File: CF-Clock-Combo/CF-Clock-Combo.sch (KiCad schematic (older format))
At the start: 15 parts, among them J1 IDE_CONNECTOR, J2 CF Adapter Power, J3 Jumpers, J4 Bus_ISA_8bit, U1 BIOS FLASH, U2 74HCT245, U3 GAL22V10, U4 DS1315, Y1 32.768 KHz

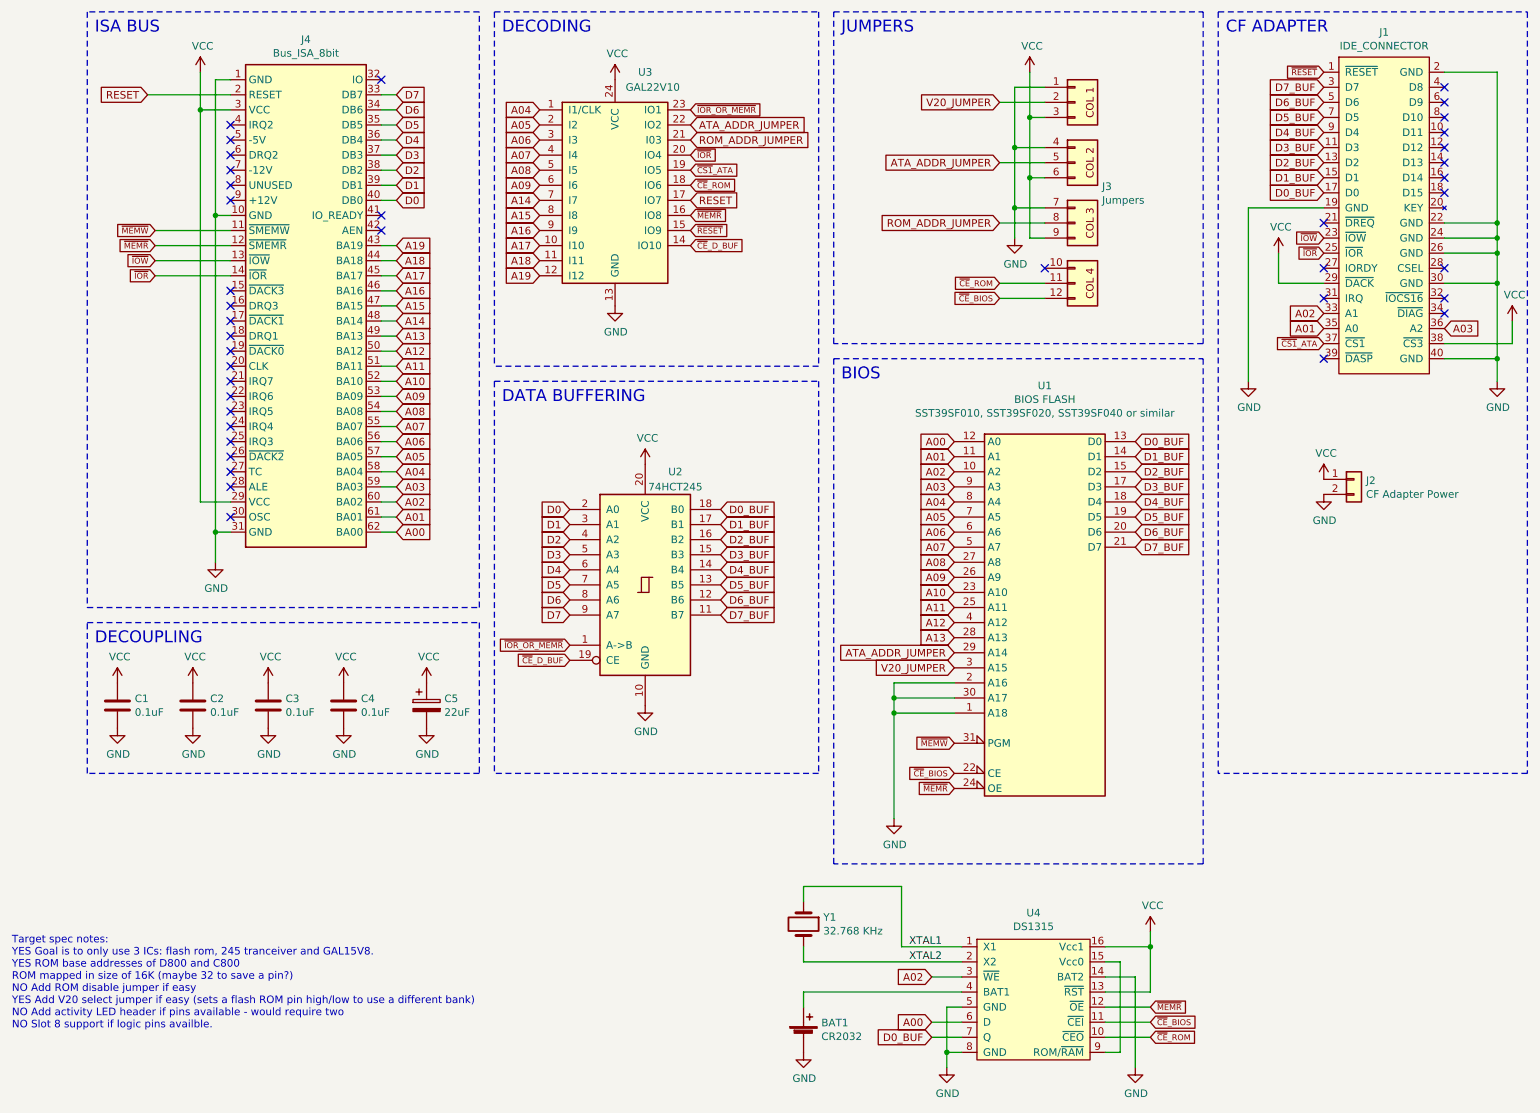
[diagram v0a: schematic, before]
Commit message: CF-Clock-Combo: Tidy up schematic.
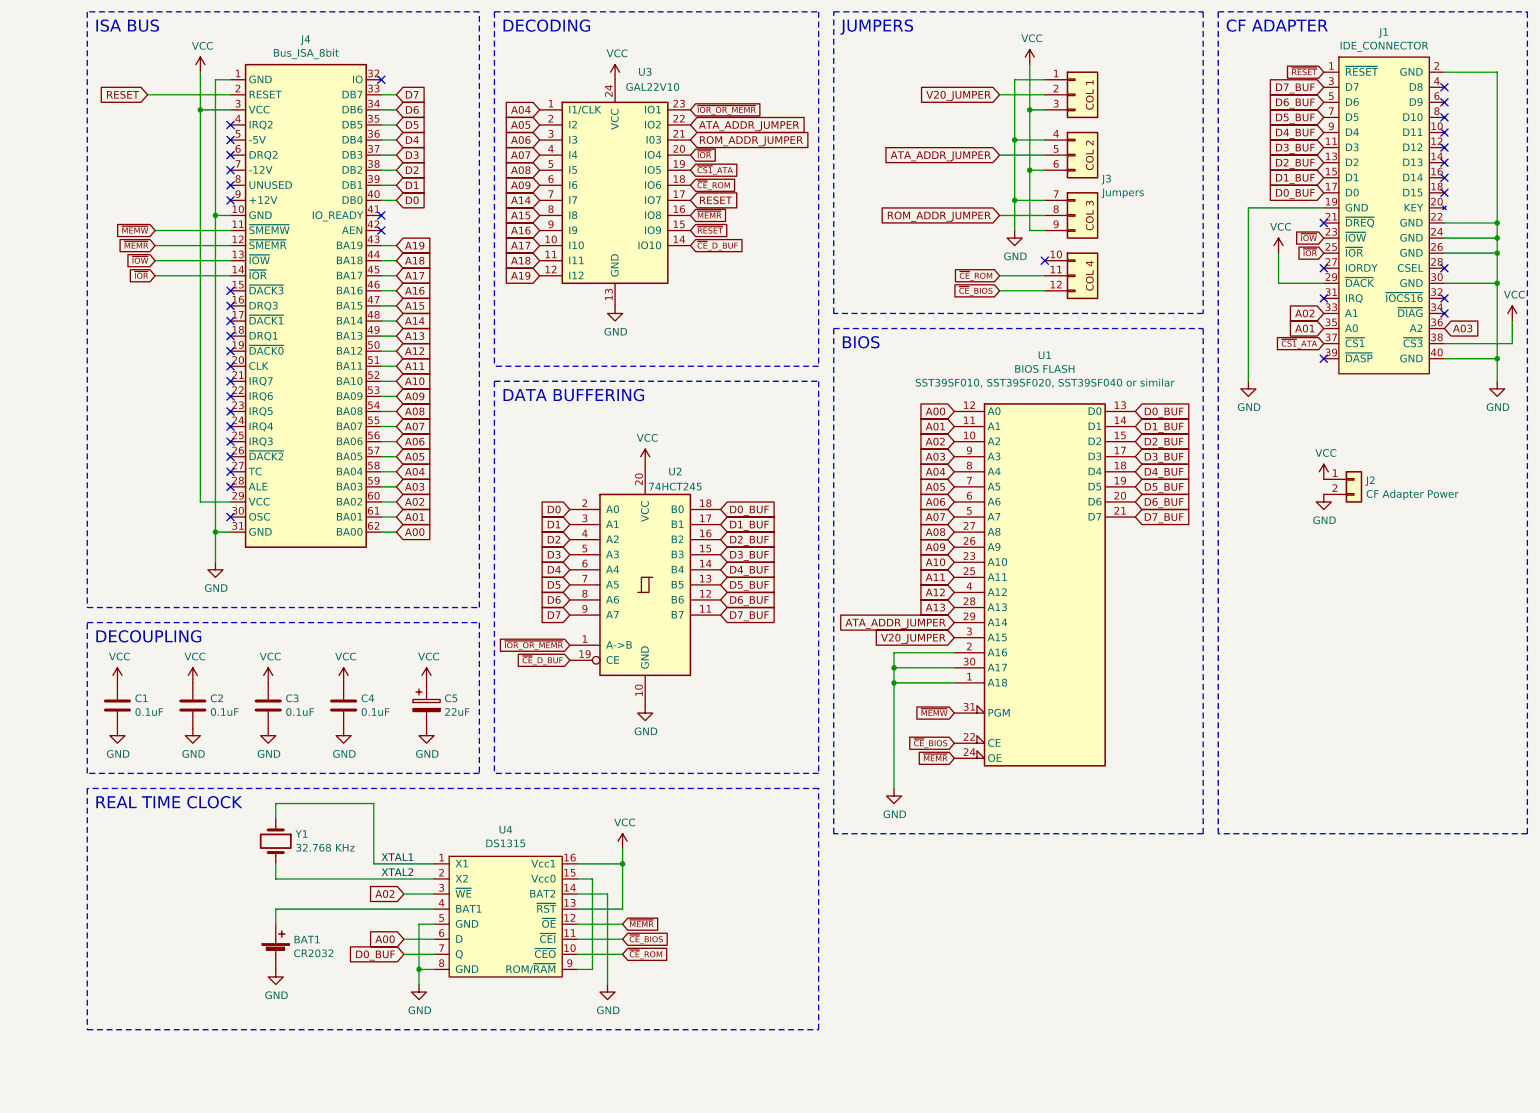
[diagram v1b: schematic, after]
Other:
- note added: "REAL TIME CLOCK"
- note removed: "Target spec notes:\nYES Goal is to only use 3 ICs: flash rom, 245 tranceiver and GAL15V8.\nYES ROM base addresses of D800 and C800\nROM mapped in size of 16K (maybe 32 to save a pin?)\nNO Add ROM disable jumper if easy\nYES Add V20 select jumper if easy (sets a flash ROM pin high/low to use a different bank)\nNO Add activity LED header if pins available - would require two\nNO Slot 8 support if l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"
- moved on the sheet: BAT1, J3, U1, U4, Y1

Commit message: Fix location of CF adapter power for all boards that use it. Also the mounting holes in the schematic for the same boards. Finishing touches to Tandy 1000 Essentials.
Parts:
- added H1, H2, H3, H4: MountingHole_Pad, MountingHole:MountingHole_3.5mm_Pad, symbol Mechanical:MountingHole_Pad
- J2: footprint Connector_PinHeader_2.54mm:PinHeader_1x02_P2.54mm_Vertical -> Connector_PinSocket_2.54mm:PinSocket_1x01_P2.54mm_Vertical; symbol Connector_Generic:Conn_01x02 -> Connector_Generic:Conn_01x01
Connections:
- net GND: now also H1.1, H2.1, H3.1, H4.1; no longer J2.2 (Pin_2)
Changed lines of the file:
@@
 $EndComp
 $Comp
-L Connector_Generic:Conn_01x02 J2
+L Connector_Generic:Conn_01x01 J2
 U 1 1 603E8D26
 P 9450 4050
 F 0 "J2" H 9530 4042 50  0000 L CNN
 F 1 "CF Adapter Power" H 9530 3951 50  0000 L CNN
-F 2 "Connector_PinHeader_2.54mm:PinHeader_1x02_P2.54mm_Vertical" H 9450 4050 50  0001 C CNN
+F 2 "Connector_PinSocket_2.54mm:PinSocket_1x01_P2.54mm_Vertical" H 9450 4050 50  0001 C CNN
 F 3 "~" H 9450 4050 50  0001 C CNN
 	1    9450 4050
-	1    0    0    -1
-$EndComp
-$Comp
-L power:GND #PWR0123
-U 1 1 603E9698
-P 9250 4150
-F 0 "#PWR0123" H 9250 3900 50  0001 C CNN
-F 1 "GND" H 9255 3977 50  0000 C CNN
-F 2 "" H 9250 4150 50  0001 C CNN
-F 3 "" H 9250 4150 50  0001 C CNN
-	1    9250 4150
 	1    0    0    -1
 $EndComp
@@
 Text Notes 1100 6250 0    79   ~ 0
 REAL TIME CLOCK
+$Comp
+L Mechanical:MountingHole_Pad H1
+U 1 1 6091DBFC
+P 9400 4850
+F 0 "H1" V 9354 5000 50  0000 L CNN
+F 1 "MountingHole_Pad" V 9445 5000 50  0000 L CNN
+F 2 "MountingHole:MountingHole_3.5mm_Pad" H 9400 4850 50  0001 C CNN
+F 3 "~" H 9400 4850 50  0001 C CNN
+	1    9400 4850
+	0    1    1    0
+$EndComp
+$Comp
+L Mechanical:MountingHole_Pad H2
+U 1 1 6091E4CA
+P 9400 5050
+F 0 "H2" V 9354 5200 50  0000 L CNN
+F 1 "MountingHole_Pad" V 9445 5200 50  0000 L CNN
+F 2 "MountingHole:MountingHole_3.5mm_Pad" H 9400 5050 50  0001 C CNN
+F 3 "~" H 9400 5050 50  0001 C CNN
+	1    9400 5050
+	0    1    1    0
+$EndComp
+$Comp
+L Mechanical:MountingHole_Pad H3
+U 1 1 6091E66C
+P 9400 5250
+F 0 "H3" V 9354 5400 50  0000 L CNN
+F 1 "MountingHole_Pad" V 9445 5400 50  0000 L CNN
+F 2 "MountingHole:MountingHole_3.5mm_Pad" H 9400 5250 50  0001 C CNN
+F 3 "~" H 9400 5250 50  0001 C CNN
+	1    9400 5250
+	0    1    1    0
+$EndComp
+$Comp
+L Mechanical:MountingHole_Pad H4
+U 1 1 6091E800
+P 9400 5450
+F 0 "H4" V 9354 5600 50  0000 L CNN
+F 1 "MountingHole_Pad" V 9445 5600 50  0000 L CNN
+F 2 "MountingHole:MountingHole_3.5mm_Pad" H 9400 5450 50  0001 C CNN
+F 3 "~" H 9400 5450 50  0001 C CNN
+	1    9400 5450
+	0    1    1    0
+$EndComp
+Wire Wire Line
+	9300 4850 9200 4850
+Wire Wire Line
+	9200 4850 9200 5050
+Wire Wire Line
+	9200 5450 9300 5450
+Connection ~ 9200 5450
+Wire Wire Line
+	9200 5450 9200 5550
+Wire Wire Line
+	9300 5250 9200 5250
+Connection ~ 9200 5250
+Wire Wire Line
+	9200 5250 9200 5450
+Wire Wire Line
+	9200 5050 9300 5050
+Connection ~ 9200 5050
+Wire Wire Line
+	9200 5050 9200 5250
+$Comp
+L power:GND #PWR01
+U 1 1 6092F423
+P 9200 5550
+F 0 "#PWR01" H 9200 5300 50  0001 C CNN
+F 1 "GND" H 9205 5377 50  0000 C CNN
+F 2 "" H 9200 5550 50  0001 C CNN
+F 3 "" H 9200 5550 50  0001 C CNN
+	1    9200 5550
+	1    0    0    -1
+$EndComp
 $EndSCHEMATC
